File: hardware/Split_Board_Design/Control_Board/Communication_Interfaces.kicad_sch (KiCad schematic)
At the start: 50 parts, among them Q2 2SD882, Q5 2SD882, Q6 2SD882, U1 TCAN3414DR, U10 LTV-356T, U11 LTV-356T, U12 LTV-356T, U14 LTV-356T, U3 MAX3485, U6 LTV-356T

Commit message: feat(layout): Finished demo schematic for control board
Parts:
- C40, C41: value 100nF - 50V -> 100nF-50V
- D12: Link to Buy (none) -> https://www.lcsc.com/product-detail/C20345391.html?s_z=n_q_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
- R61: Link to Buy (none) -> https://linhkien.cxtvn.com/1422-dien-tro-10k-0603-1-100c.ht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
- R62: Link to Buy (none) -> https://linhkien.cxtvn.com/4434-dien-tro-15k-0603-1-100c.ht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
- R74, R77, R80: Link to Buy https://linhkien.cxtvn.com/2289-dien-tro-33k-0603-1-100c.ht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 -> https://linhkien.cxtvn.com/1424-dien-tro-1k-0603-1-100c.html
- R76, R79: Link to Buy https://linhkien.cxtvn.com/9909-dien-tro-0805-05-18w-10-chi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 -> https://linhkien.cxtvn.com/1422-dien-tro-10k-0603-1-100c.ht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
- U1: Link to Buy (none) -> https://www.lcsc.com/product-image/C22396693.html?whichImg=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

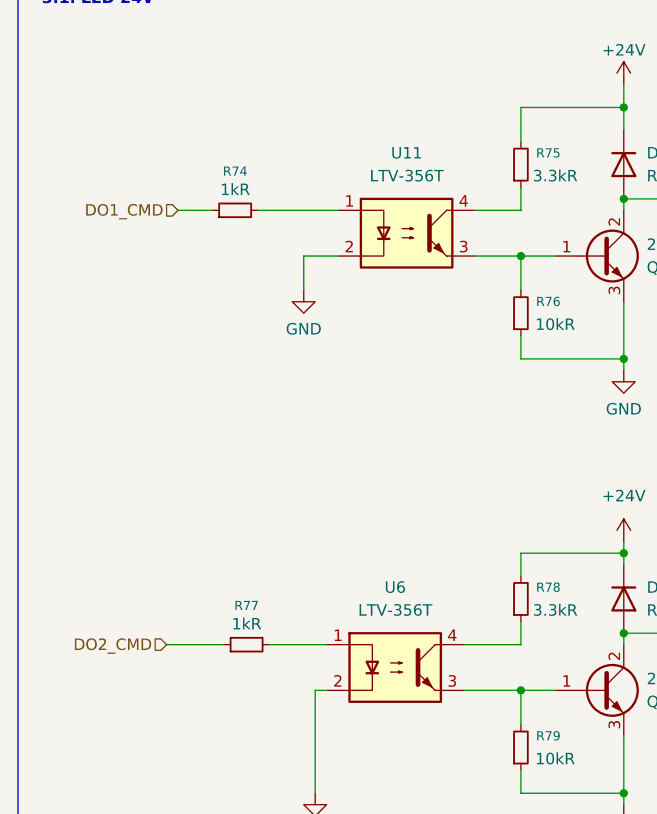
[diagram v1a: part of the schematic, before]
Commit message: feat(layout): update control board layout
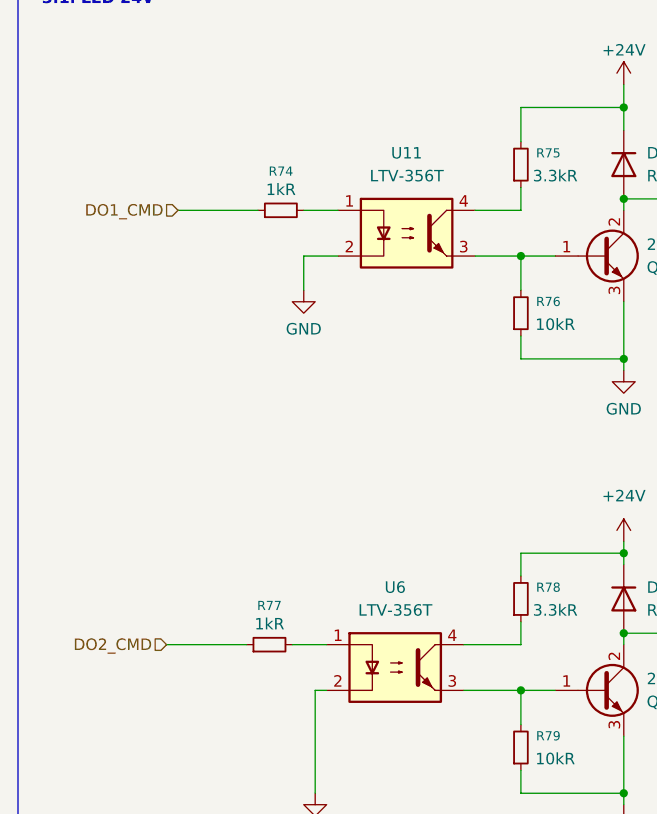
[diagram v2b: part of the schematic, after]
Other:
- moved on the sheet: R74, R77
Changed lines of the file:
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@@
 	(wire
 		(pts
-			(xy 33.02 110.49) (xy 36.83 110.49)
+			(xy 33.02 110.49) (xy 41.91 110.49)
 		)
 		(stroke
@@
 	(wire
 		(pts
-			(xy 31.75 158.75) (xy 38.1 158.75)
+			(xy 31.75 158.75) (xy 40.64 158.75)
 		)
 		(stroke
@@
 	(wire
 		(pts
-			(xy 41.91 110.49) (xy 50.8 110.49)
+			(xy 46.99 110.49) (xy 50.8 110.49)
 		)
 		(stroke
@@
 	(wire
 		(pts
-			(xy 43.18 158.75) (xy 49.53 158.75)
+			(xy 45.72 158.75) (xy 49.53 158.75)
 		)
 		(stroke
@@
 	(symbol
 		(lib_id "Device:R_Small")
-		(at 40.64 158.75 90)
+		(at 43.18 158.75 90)
 		(unit 1)
 		(body_style 1)
@@
 		(dnp no)
 		(property "Reference" "R77"
-			(at 40.64 154.432 90)
+			(at 43.18 154.432 90)
 			(show_name no)
 			(do_not_autoplace no)
@@
 		)
 		(property "Value" "1kR"
-			(at 40.64 156.464 90)
+			(at 43.18 156.464 90)
 			(show_name no)
 			(do_not_autoplace no)
@@
 		)
 		(property "Footprint" "Resistor_SMD:R_0603_1608Metric"
-			(at 40.64 158.75 0)
+			(at 43.18 158.75 0)
 			(hide yes)
 			(show_name no)
@@
 		)
 		(property "Datasheet" ""
-			(at 40.64 158.75 0)
+			(at 43.18 158.75 0)
 			(hide yes)
 			(show_name no)
@@
 		)
 		(property "Description" "Resistor, small symbol"
-			(at 40.64 158.75 0)
+			(at 43.18 158.75 0)
 			(hide yes)
 			(show_name no)
@@
 		)
 		(property "BOM Comments" ""
-			(at 40.64 158.75 90)
+			(at 43.18 158.75 90)
 			(hide yes)
 			(show_name no)
@@
 		)
 		(property "DigiKey_Part_Number" ""
-			(at 40.64 158.75 90)
+			(at 43.18 158.75 90)
 			(hide yes)
 			(show_name no)
@@
 		)
 		(property "Link" ""
-			(at 40.64 158.75 90)
+			(at 43.18 158.75 90)
 			(hide yes)
 			(show_name no)
@@
 		)
 		(property "Sim.Type" ""
-			(at 40.64 158.75 90)
+			(at 43.18 158.75 90)
 			(hide yes)
 			(show_name no)
@@
 		)
 		(property "VENDOR" ""
-			(at 40.64 158.75 90)
+			(at 43.18 158.75 90)
 			(hide yes)
 			(show_name no)
@@
 		)
 		(property "Link to Buy" "https://linhkien.cxtvn.com/1424-dien-tro-1k-0603-1-100c.html"
-			(at 0 0 0)
+			(at 2.54 0 0)
 			(hide yes)
 			(show_name no)
@@
 		)
 		(property "CREATOR" ""
-			(at 40.64 158.75 90)
+			(at 43.18 158.75 90)
 			(hide yes)
 			(show_name no)
@@
 	(symbol
 		(lib_id "Device:R_Small")
-		(at 39.37 110.49 90)
+		(at 44.45 110.49 90)
 		(unit 1)
 		(body_style 1)
@@
 		(dnp no)
 		(property "Reference" "R74"
-			(at 39.37 106.172 90)
+			(at 44.45 106.172 90)
 			(show_name no)
 			(do_not_autoplace no)
@@
 		)
 		(property "Value" "1kR"
-			(at 39.37 108.204 90)
+			(at 44.45 108.204 90)
 			(show_name no)
 			(do_not_autoplace no)
@@
 		)
 		(property "Footprint" "Resistor_SMD:R_0603_1608Metric"
-			(at 39.37 110.49 0)
+			(at 44.45 110.49 0)
 			(hide yes)
 			(show_name no)
@@
 		)
 		(property "Datasheet" ""
-			(at 39.37 110.49 0)
+			(at 44.45 110.49 0)
 			(hide yes)
 			(show_name no)
@@
 		)
 		(property "Description" "Resistor, small symbol"
-			(at 39.37 110.49 0)
+			(at 44.45 110.49 0)
 			(hide yes)
 			(show_name no)
@@
 		)
 		(property "BOM Comments" ""
-			(at 39.37 110.49 90)
+			(at 44.45 110.49 90)
 			(hide yes)
 			(show_name no)
@@
 		)
 		(property "DigiKey_Part_Number" ""
-			(at 39.37 110.49 90)
+			(at 44.45 110.49 90)
 			(hide yes)
 			(show_name no)
@@
 		)
 		(property "Link" ""
-			(at 39.37 110.49 90)
+			(at 44.45 110.49 90)
 			(hide yes)
 			(show_name no)
@@
 		)
 		(property "Sim.Type" ""
-			(at 39.37 110.49 90)
+			(at 44.45 110.49 90)
 			(hide yes)
 			(show_name no)
@@
 		)
 		(property "VENDOR" ""
-			(at 39.37 110.49 90)
+			(at 44.45 110.49 90)
 			(hide yes)
 			(show_name no)
@@
 		)
 		(property "Link to Buy" "https://linhkien.cxtvn.com/1424-dien-tro-1k-0603-1-100c.html"
-			(at -1.27 0 0)
+			(at 3.81 0 0)
 			(hide yes)
 			(show_name no)
@@
 		)
 		(property "CREATOR" ""
-			(at 39.37 110.49 90)
+			(at 44.45 110.49 90)
 			(hide yes)
 			(show_name no)

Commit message: layout: update layout
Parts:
- D12: MPN SM712 -> ESD2CANFD24DBZR; Manufacturer Littelfuse/Semtech -> (none)
- D19, D23: footprint Diode_SMD:D_SOD-323 -> Diode_SMD:D_SOD-523; LCSC Part C96512 -> (none); Link to Buy https://linhkienthuduc.com/san-pham/pesd5z3-3/ -> (none); MPN PESD5Z3.3 -> (none); Manufacturer Nexperia -> (none)
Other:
- moved on the sheet: D1
